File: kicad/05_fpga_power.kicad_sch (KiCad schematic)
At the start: 70 parts, among them U501 Ti135N484I3

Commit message: U501 100n decaps to 0201, placed straight on rail/GND via pairs
- 05_fpga_power: the 37 x 100n are C_0201_0603Metric (e.g. GRM033R60J104KE19D / LCSC C76928,
  JLC extended, ample stock). On U501's 0.8 mm via-in-pad grid neither 0201 nor 0402 fits between
  the vias, but an 0201 sits with its pads on an adjacent rail/GND via pair: the shortest loop.
- tools/swap_footprint.py: footprint swap on the board keeping nets, fields, schematic link.
- tools/place_bga_decaps.py: each cap onto a pair of its own rail (pad 1 on the rail via), spread
  over the rail's pairs; clearance checked against vias (copper and hole), B.Cu tracks, pads and
  courtyards. VCORE 9/9, 0V85 5/5, 1V1 8/8, 1V8 5/7 on pairs; 3V3 (no pairs) and two 1V8 stay.
  The 1u/4u7 0402s under U501 took remaining pairs or the nearest free spot.
- KiCad DRC with schematic parity: no new errors; LPDDR4 untouched.

Co-Authored-By: Claude Opus 5.5 <noreply@anthropic.com>
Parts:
- C515, C516, C517, C518, C519, C520, C521, C522, C523, C524, C525, C526, C532, C533, C534, C535, C536, C537, C543, C544, C545, C546, C547, C548, C549, C550, C554, C555, C556, C557, C558, C559, C560, C561, C563, C564, C565: footprint Capacitor_SMD:C_0402_1005Metric -> Capacitor_SMD:C_0201_0603Metric
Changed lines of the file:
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@@
 			)
 		)
-		(property "Footprint" "Capacitor_SMD:C_0402_1005Metric"
+		(property "Footprint" "Capacitor_SMD:C_0201_0603Metric"
 			(at 92.4052 146.05 0)
 			(effects
@@
 			)
 		)
-		(property "Footprint" "Capacitor_SMD:C_0402_1005Metric"
+		(property "Footprint" "Capacitor_SMD:C_0201_0603Metric"
 			(at 101.2952 146.05 0)
 			(effects
@@
 			)
 		)
-		(property "Footprint" "Capacitor_SMD:C_0402_1005Metric"
+		(property "Footprint" "Capacitor_SMD:C_0201_0603Metric"
 			(at 110.1852 146.05 0)
 			(effects
@@
 			)
 		)
-		(property "Footprint" "Capacitor_SMD:C_0402_1005Metric"
+		(property "Footprint" "Capacitor_SMD:C_0201_0603Metric"
 			(at 119.0752 146.05 0)
 			(effects
@@
 			)
 		)
-		(property "Footprint" "Capacitor_SMD:C_0402_1005Metric"
+		(property "Footprint" "Capacitor_SMD:C_0201_0603Metric"
 			(at 127.9652 146.05 0)
 			(effects
@@
 			)
 		)
-		(property "Footprint" "Capacitor_SMD:C_0402_1005Metric"
+		(property "Footprint" "Capacitor_SMD:C_0201_0603Metric"
 			(at 136.8552 146.05 0)
 			(effects
@@
 			)
 		)
-		(property "Footprint" "Capacitor_SMD:C_0402_1005Metric"
+		(property "Footprint" "Capacitor_SMD:C_0201_0603Metric"
 			(at 145.7452 146.05 0)
 			(effects
@@
 			)
 		)
-		(property "Footprint" "Capacitor_SMD:C_0402_1005Metric"
+		(property "Footprint" "Capacitor_SMD:C_0201_0603Metric"
 			(at 154.6352 146.05 0)
 			(effects
@@
 			)
 		)
-		(property "Footprint" "Capacitor_SMD:C_0402_1005Metric"
+		(property "Footprint" "Capacitor_SMD:C_0201_0603Metric"
 			(at 163.5252 146.05 0)
 			(effects
@@
 			)
 		)
-		(property "Footprint" "Capacitor_SMD:C_0402_1005Metric"
+		(property "Footprint" "Capacitor_SMD:C_0201_0603Metric"
 			(at 172.4152 146.05 0)
 			(effects
@@
 			)
 		)
-		(property "Footprint" "Capacitor_SMD:C_0402_1005Metric"
+		(property "Footprint" "Capacitor_SMD:C_0201_0603Metric"
 			(at 181.3052 146.05 0)
 			(effects
@@
 			)
 		)
-		(property "Footprint" "Capacitor_SMD:C_0402_1005Metric"
+		(property "Footprint" "Capacitor_SMD:C_0201_0603Metric"
 			(at 190.1952 146.05 0)
 			(effects
@@
 			)
 		)
-		(property "Footprint" "Capacitor_SMD:C_0402_1005Metric"
+		(property "Footprint" "Capacitor_SMD:C_0201_0603Metric"
 			(at 83.5152 179.07 0)
 			(effects
@@
 			)
 		)
-		(property "Footprint" "Capacitor_SMD:C_0402_1005Metric"
+		(property "Footprint" "Capacitor_SMD:C_0201_0603Metric"
 			(at 92.4052 179.07 0)
 			(effects
@@
 			)
 		)
-		(property "Footprint" "Capacitor_SMD:C_0402_1005Metric"
+		(property "Footprint" "Capacitor_SMD:C_0201_0603Metric"
 			(at 101.2952 179.07 0)
 			(effects
@@
 			)
 		)
-		(property "Footprint" "Capacitor_SMD:C_0402_1005Metric"
+		(property "Footprint" "Capacitor_SMD:C_0201_0603Metric"
 			(at 110.1852 179.07 0)
 			(effects
@@
 			)
 		)
-		(property "Footprint" "Capacitor_SMD:C_0402_1005Metric"
+		(property "Footprint" "Capacitor_SMD:C_0201_0603Metric"
 			(at 119.0752 179.07 0)
 			(effects
@@
 			)
 		)
-		(property "Footprint" "Capacitor_SMD:C_0402_1005Metric"
+		(property "Footprint" "Capacitor_SMD:C_0201_0603Metric"
 			(at 127.9652 179.07 0)
 			(effects
@@
 			)
 		)
-		(property "Footprint" "Capacitor_SMD:C_0402_1005Metric"
+		(property "Footprint" "Capacitor_SMD:C_0201_0603Metric"
 			(at 83.5152 212.09 0)
 			(effects
@@
 			)
 		)
-		(property "Footprint" "Capacitor_SMD:C_0402_1005Metric"
+		(property "Footprint" "Capacitor_SMD:C_0201_0603Metric"
 			(at 92.4052 212.09 0)
 			(effects
@@
 			)
 		)
-		(property "Footprint" "Capacitor_SMD:C_0402_1005Metric"
+		(property "Footprint" "Capacitor_SMD:C_0201_0603Metric"
 			(at 101.2952 212.09 0)
 			(effects
@@
 			)
 		)
-		(property "Footprint" "Capacitor_SMD:C_0402_1005Metric"
+		(property "Footprint" "Capacitor_SMD:C_0201_0603Metric"
 			(at 110.1852 212.09 0)
 			(effects
@@
 			)
 		)
-		(property "Footprint" "Capacitor_SMD:C_0402_1005Metric"
+		(property "Footprint" "Capacitor_SMD:C_0201_0603Metric"
 			(at 119.0752 212.09 0)
 			(effects
@@
 			)
 		)
-		(property "Footprint" "Capacitor_SMD:C_0402_1005Metric"
+		(property "Footprint" "Capacitor_SMD:C_0201_0603Metric"
 			(at 127.9652 212.09 0)
 			(effects
@@
 			)
 		)
-		(property "Footprint" "Capacitor_SMD:C_0402_1005Metric"
+		(property "Footprint" "Capacitor_SMD:C_0201_0603Metric"
 			(at 136.8552 212.09 0)
 			(effects
@@
 			)
 		)
-		(property "Footprint" "Capacitor_SMD:C_0402_1005Metric"
+		(property "Footprint" "Capacitor_SMD:C_0201_0603Metric"
 			(at 145.7452 212.09 0)
 			(effects
@@
 			)
 		)
-		(property "Footprint" "Capacitor_SMD:C_0402_1005Metric"
+		(property "Footprint" "Capacitor_SMD:C_0201_0603Metric"
 			(at 287.9852 222.25 0)
 			(effects
@@
 			)
 		)
-		(property "Footprint" "Capacitor_SMD:C_0402_1005Metric"
+		(property "Footprint" "Capacitor_SMD:C_0201_0603Metric"
 			(at 296.8752 222.25 0)
 			(effects
@@
 			)
 		)
-		(property "Footprint" "Capacitor_SMD:C_0402_1005Metric"
+		(property "Footprint" "Capacitor_SMD:C_0201_0603Metric"
 			(at 305.7652 222.25 0)
 			(effects
@@
 			)
 		)
-		(property "Footprint" "Capacitor_SMD:C_0402_1005Metric"
+		(property "Footprint" "Capacitor_SMD:C_0201_0603Metric"
 			(at 314.6552 222.25 0)
 			(effects
@@
 			)
 		)
-		(property "Footprint" "Capacitor_SMD:C_0402_1005Metric"
+		(property "Footprint" "Capacitor_SMD:C_0201_0603Metric"
 			(at 323.5452 222.25 0)
 			(effects
@@
 			)
 		)
-		(property "Footprint" "Capacitor_SMD:C_0402_1005Metric"
+		(property "Footprint" "Capacitor_SMD:C_0201_0603Metric"
 			(at 332.4352 222.25 0)
 			(effects
@@
 			)
 		)
-		(property "Footprint" "Capacitor_SMD:C_0402_1005Metric"
+		(property "Footprint" "Capacitor_SMD:C_0201_0603Metric"
 			(at 341.3252 222.25 0)
 			(effects
@@
 			)
 		)
-		(property "Footprint" "Capacitor_SMD:C_0402_1005Metric"
+		(property "Footprint" "Capacitor_SMD:C_0201_0603Metric"
 			(at 350.2152 222.25 0)
 			(effects
@@
 			)
 		)
-		(property "Footprint" "Capacitor_SMD:C_0402_1005Metric"
+		(property "Footprint" "Capacitor_SMD:C_0201_0603Metric"
 			(at 270.2052 255.27 0)
 			(effects
@@
 			)
 		)
-		(property "Footprint" "Capacitor_SMD:C_0402_1005Metric"
+		(property "Footprint" "Capacitor_SMD:C_0201_0603Metric"
 			(at 279.0952 255.27 0)
 			(effects
@@
 			)
 		)
-		(property "Footprint" "Capacitor_SMD:C_0402_1005Metric"
+		(property "Footprint" "Capacitor_SMD:C_0201_0603Metric"
 			(at 287.9852 255.27 0)
 			(effects

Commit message: Phase 3 (half): checklist fixes in the schematic; board placement still to do
- R801 240R 0.1 % (RT0402BRD07240RL, C852660); SSU_N (L4) 10 k pull-up R622 to 1V8.
- Efinix decoupling table in full on sheet 05 (now A2): C5001-C5073 (0201 10n/1n/100n,
  0402 1u/4u7, 0805 10u/47u, 1206 100u).
- Each TLV62585 cell: 47u output cap and a 22p feed-forward cap across R1 (data sheet:
  feed-forward needed above 47 uF; user decision).
- build_schematic.sh fails on duplicate references (ERC misses them).
- tools/add_parts.py: add missing schematic parts to a routed board; tools/place_free.py
  (untested): nearest free B.Cu spot.
- kicad/ti135_card.kicad_pcb unchanged; placement in work/p3, see NEXT_SESSION.md.

Co-Authored-By: Claude Opus 5.5 <noreply@anthropic.com>
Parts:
- added C5001, C5002: 100u, Capacitor_SMD:C_1206_3216Metric, symbol ti135_card:C
- added C5003, C5019, C5020, C5021, C5022: 47u, Capacitor_SMD:C_0805_2012Metric, symbol ti135_card:C
- added C5004, C5005, C5023, C5024, C5025, C5026: 10u, Capacitor_SMD:C_0805_2012Metric, symbol ti135_card:C
- added C5006, C5007, C5008, C5031, C5032, C5033, C5034, C5035, C5050, C5051, C5052: 1u, Capacitor_SMD:C_0402_1005Metric, symbol ti135_card:C
- added C5009, C5010, C5011, C5012, C5013, C5014, C5015, C5036, C5037, C5038, C5039, C5040, C5041, C5053, C5057, C5058, C5059, C5061, C5062, C5065, C5066, C5069, C5070, C5072: 10n, Capacitor_SMD:C_0201_0603Metric, symbol ti135_card:C
- added C5016, C5017, C5018, C5042, C5043, C5044, C5045, C5046, C5047, C5063, C5067, C5071, C5073: 1n, Capacitor_SMD:C_0201_0603Metric, symbol ti135_card:C
- added C5027, C5028, C5029, C5030, C5048, C5049, C5054, C5055, C5056: 4u7, Capacitor_SMD:C_0402_1005Metric, symbol ti135_card:C
- added C5060, C5064, C5068: 100n, Capacitor_SMD:C_0201_0603Metric, symbol ti135_card:C
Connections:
- net 0V85: now also C5053.1
- net 1V1: now also C5054.1, C5055.1, C5056.1, C5057.1, C5058.1, C5059.1
- net 1V8: now also C5019.1, C5020.1, C5021.1, C5022.1, C5023.1, C5024.1, C5025.1, C5026.1, C5027.1, C5028.1, C5029.1, C5030.1, C5031.1, C5032.1, C5033.1, C5034.1, C5035.1, C5036.1, C5037.1, C5038.1, C5039.1, C5040.1, C5041.1, C5042.1, C5043.1, C5044.1, C5045.1, C5046.1, C5047.1
- net 3V3: now also C5048.1, C5049.1, C5050.1, C5051.1, C5052.1
- net GND: now also C5001.2, C5002.2, C5003.2, C5004.2, C5005.2, C5006.2, C5007.2, C5008.2, C5009.2, C5010.2, C5011.2, C5012.2, C5013.2, C5014.2, C5015.2, C5016.2, C5017.2, C5018.2, C5019.2, C5020.2, C5021.2, C5022.2, C5023.2, C5024.2, C5025.2, C5026.2, C5027.2, C5028.2, C5029.2, C5030.2, C5031.2, C5032.2, C5033.2, C5034.2, C5035.2, C5036.2, C5037.2, C5038.2, C5039.2, C5040.2, C5041.2, C5042.2, C5043.2, C5044.2, C5045.2, C5046.2, C5047.2, C5048.2, C5049.2, C5050.2, C5051.2, C5052.2, C5053.2, C5054.2, C5055.2, C5056.2, C5057.2, C5058.2, C5059.2, C5060.2, C5061.2, C5062.2, C5063.2, C5064.2, C5065.2, C5066.2, C5067.2, C5068.2, C5069.2, C5070.2, C5071.2, C5072.2, C5073.2
- net VCORE: now also C5001.1, C5002.1, C5003.1, C5004.1, C5005.1, C5006.1, C5007.1, C5008.1, C5009.1, C5010.1, C5011.1, C5012.1, C5013.1, C5014.1, C5015.1, C5016.1, C5017.1, C5018.1
- net vcca_bl: now also C5060.1, C5061.1, C5062.1, C5063.1
- net vcca_br: now also C5064.1, C5065.1, C5066.1, C5067.1
- net vcca_tr: now also C5068.1, C5069.1, C5070.1, C5071.1
- net vddpll_mcb_top_phy_ddr: now also C5072.1, C5073.1
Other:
- note added: "0V85 VDD_PHY, checklist addition: 10n"
- note added: "1V1, checklist additions: 3 x 4u7, 3 x 10n"
- note added: "1V8, checklist additions (VCCIO x 5 banks + VCCAUX): 4 x 47u (+ C304), 4 x 10u, 4 x 4u7, 5 x 1u"
- note added: "1V8, checklist additions: 6 x 10n, 6 x 1n"
- note added: "3V3, checklist additions (VCCIO33 x 3 banks): 2 x 4u7, 3 x 1u"
- note added: "VCORE, checklist additions: 2 x 100u, 47u (+ C204), 2 x 10u, 3 x 1u, 7 x 10n, 3 x 1n"
- note added: "vcca_bl, checklist additions"
- note added: "vcca_br, checklist additions"
- note added: "vcca_tr, checklist additions"
- note added: "vddpll_mcb_top_phy_ddr, checklist additions"

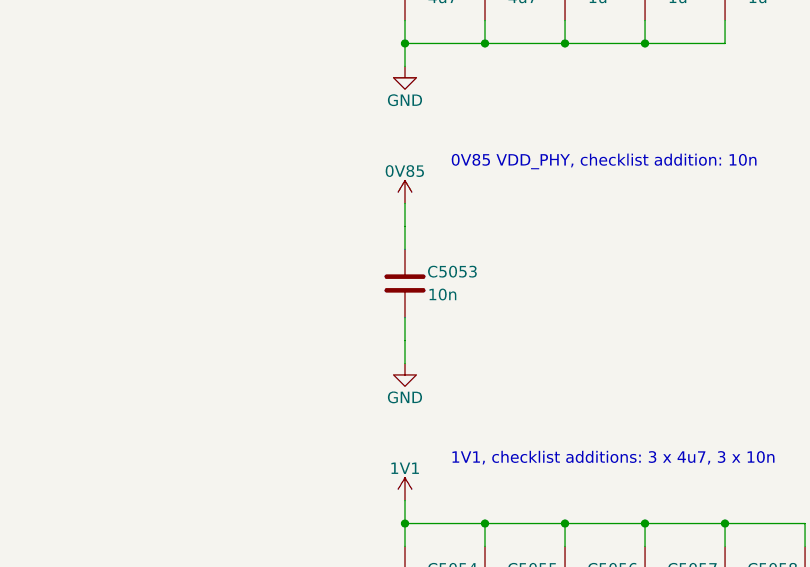
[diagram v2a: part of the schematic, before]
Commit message: LPDDR4 hand routing: Agilex DRAM escape copied, byte lanes routed, DQ swizzle by hand
- U801 decoupling = the Agilex U12 set (sheet 08: 29 x 100n 0201, 22u/1u 0402, LCSC from the
  Agilex card), placed at the Agilex positions on the same via pairs; R802 (ZQ) at R43's spot;
  CA/CKE T-branches on B.Cu copied (tools/ddr/copy_dram_escape.py)
- LPDDR4 vias not on a BGA ball removed (T-branch centre vias kept)
- Schematic: #PWR/#FLG references made unique per sheet (prefix = sheet number); the
  duplicates blocked Update PCB from Schematic
- DQ swizzle now edited by hand in the schematic (bytes 0 and 2); efinity/pinplan/lpddr4_swizzle.json
  is not updated yet
- Byte lanes routed by hand (work in progress)

Known open (WIP): byte 2 - ddr_dq22 on two U501 balls (AA16, W16), ddr_dq21 has no U501 ball;
DRC shows 2 shorts at U501 Y16/W16 (dq21/dq17 tracks).

Co-Authored-By: Claude Opus 5.5 <noreply@anthropic.com>
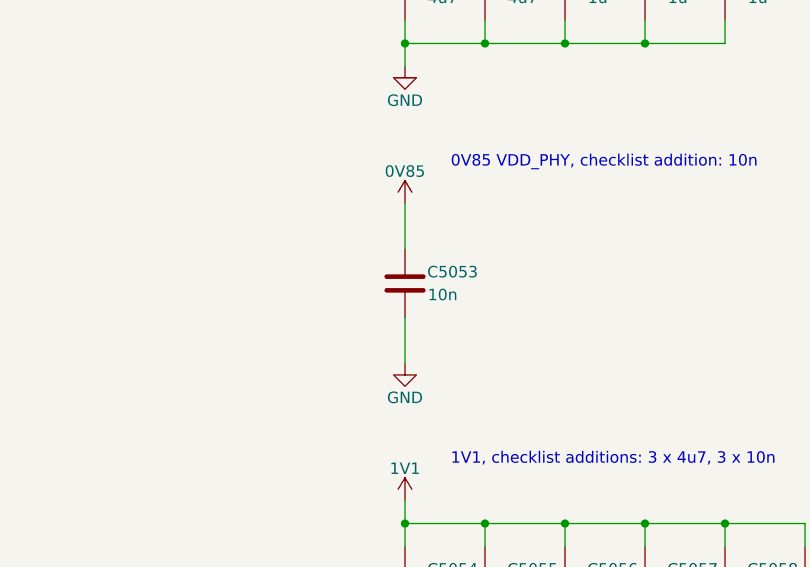
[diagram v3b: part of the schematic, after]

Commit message: LCSC numbers for all JLC parts; Y701 -> YXC OT322525MJBA4SL
- tools/set_lcsc.py: one table (value, footprint) -> LCSC, fills empty LCSC fields in the
  sheets; 312 symbols. JLC basic parts where available, cap voltages checked per rail,
  VCORE divider 0.1 % (no 0.5 % in stock). Board fields synced with add_parts.py.
- Y701: the SiT8924 has no JLC stock; now YXC OT322525MJBA4SL (C669088, 3225), EN tied
  to 1V8. R701/C701 moved 0.5 mm to clear its courtyard. Netlist change: Y701 pin 1 -> 1V8.
- Only U501 (Ti135) is left without LCSC (global sourcing / consigned).
- DRC: schematic parity 0.

Co-Authored-By: Claude Opus 5.5 <noreply@anthropic.com>
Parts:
- C5001, C5002: LCSC (none) -> C15008
- C5003, C5019, C5020, C5021, C5022: LCSC (none) -> C16780
- C5004, C5005, C5023, C5024, C5025, C5026, C527, C538, C551: LCSC (none) -> C15850
- C5006, C5007, C5008, C501, C503, C5031, C5032, C5033, C5034, C5035, C505, C5050, C5051, C5052, C507, C528, C529, C530, C531, C539, C540, C541, C542: LCSC (none) -> C52923
- C5009, C5010, C5011, C5012, C5013, C5014, C5015, C5036, C5037, C5038, C5039, C5040, C5041, C5053, C5057, C5058, C5059, C5061, C5062, C5065, C5066, C5069, C5070, C5072: LCSC (none) -> C76941
- C5016, C5017, C5018, C5042, C5043, C5044, C5045, C5046, C5047, C5063, C5067, C5071, C5073: LCSC (none) -> C66942
- C502, C504, C506, C508: LCSC (none) -> C1525
- C5027, C5028, C5029, C5030, C5048, C5049, C5054, C5055, C5056, C511, C512, C513, C514, C552, C553, C562: LCSC (none) -> C23733
- C5060, C5064, C5068, C515, C516, C517, C518, C519, C520, C521, C522, C523, C524, C525, C526, C532, C533, C534, C535, C536, C537, C543, C544, C545, C546, C547, C548, C549, C550, C554, C555, C556, C557, C558, C559, C560, C561, C563, C564, C565: LCSC (none) -> C190183
- C509, C510: LCSC (none) -> C45783
- FB501, FB502, FB503, FB504: LCSC (none) -> C88970

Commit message: 3D models for the BGAs (U501, U801, U1001, U601)
KiCad's library has no model for any of them (the footprints pointed at
missing STEP files), so tools/gen_bga_3d.py writes simple VRML models
(body, pin-1 dot, balls) to lib/3dmodels, from datasheet dimensions:
Efinix N484 model, SK hynix 200-ball FBGA, Kioxia P-WFBGA153, ISSI 24-ball
TFBGA (H). Linked as ${KIPRJMOD}/../lib/3dmodels so the CI render finds them.

U501 and U1001 footprints copied into ti135_card.pretty (footprint fields
updated on board, schematic, symbol lib); the U501 copy carries the board's
pad-to-die delays, which clears its lib_footprint_mismatch. DRC parity clean.

Co-Authored-By: Claude Opus 5.5 <noreply@anthropic.com>
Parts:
- U501: footprint Package_BGA:LFBGA-484_18x18mm_Layout22x22_P0.8mm -> ti135_card:LFBGA-484_18x18mm_Layout22x22_P0.8mm
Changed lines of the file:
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@@
 			)
 		)
-		(property "Footprint" "Package_BGA:LFBGA-484_18x18mm_Layout22x22_P0.8mm"
+		(property "Footprint" "ti135_card:LFBGA-484_18x18mm_Layout22x22_P0.8mm"
 			(at 381 139.7 0)
 			(hide yes)
@@
 			)
 		)
-		(property "Footprint" "Package_BGA:LFBGA-484_18x18mm_Layout22x22_P0.8mm"
+		(property "Footprint" "ti135_card:LFBGA-484_18x18mm_Layout22x22_P0.8mm"
 			(at 342.9 63.5 0)
 			(hide yes)
@@
 			)
 		)
-		(property "Footprint" "Package_BGA:LFBGA-484_18x18mm_Layout22x22_P0.8mm"
+		(property "Footprint" "ti135_card:LFBGA-484_18x18mm_Layout22x22_P0.8mm"
 			(at 139.7 83.82 0)
 			(hide yes)
